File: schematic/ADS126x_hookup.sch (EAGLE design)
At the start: 13 parts, among them J1 RASPBERRYPI-40-PIN-GPIO_PTH_N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

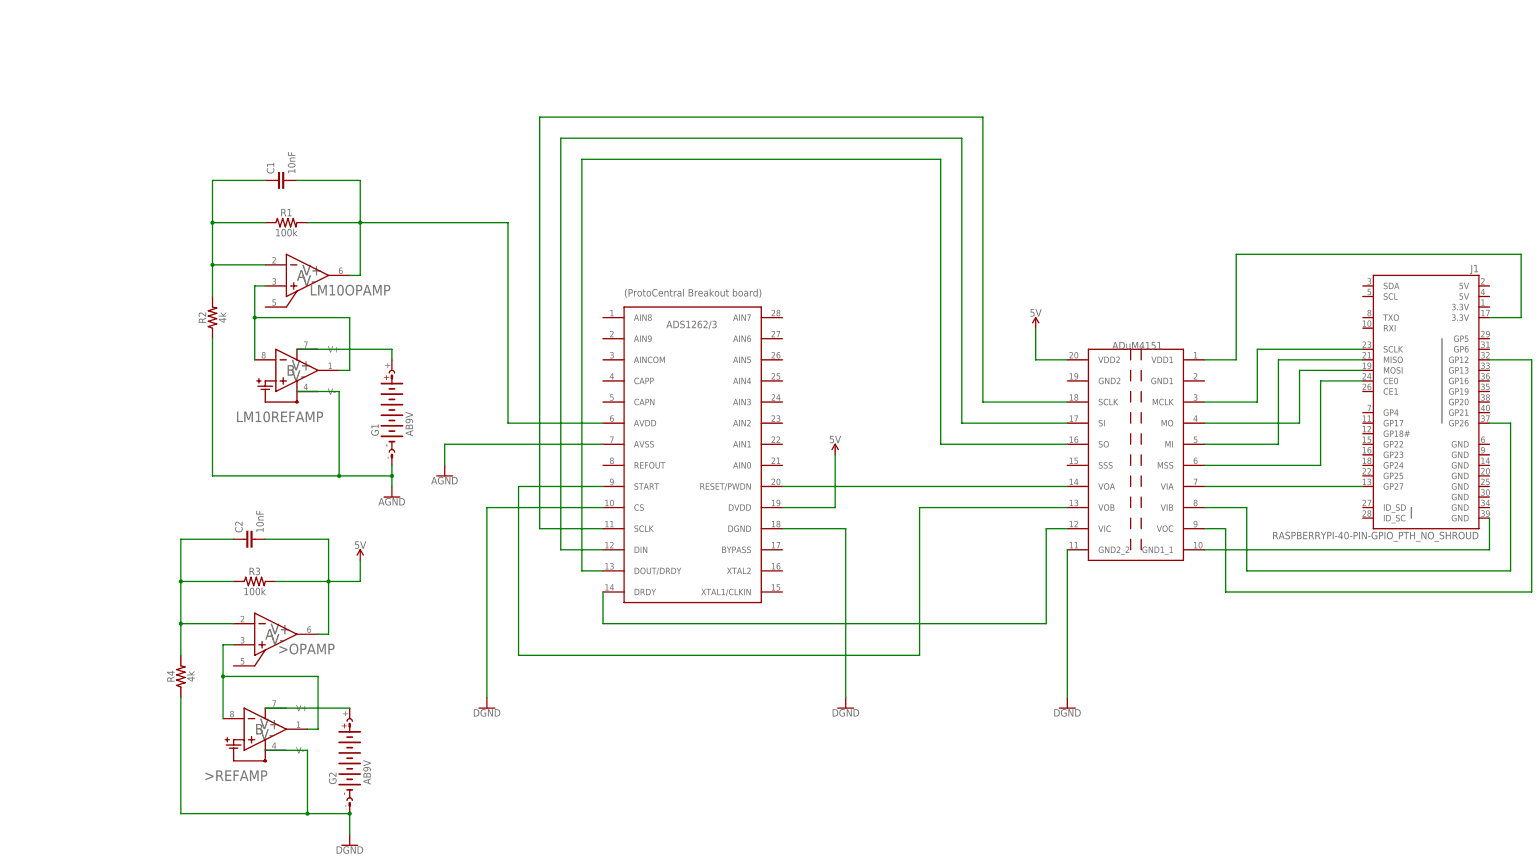
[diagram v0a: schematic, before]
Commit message: Major refactor to match Go library. updated schematic and added simplified wiring diagram
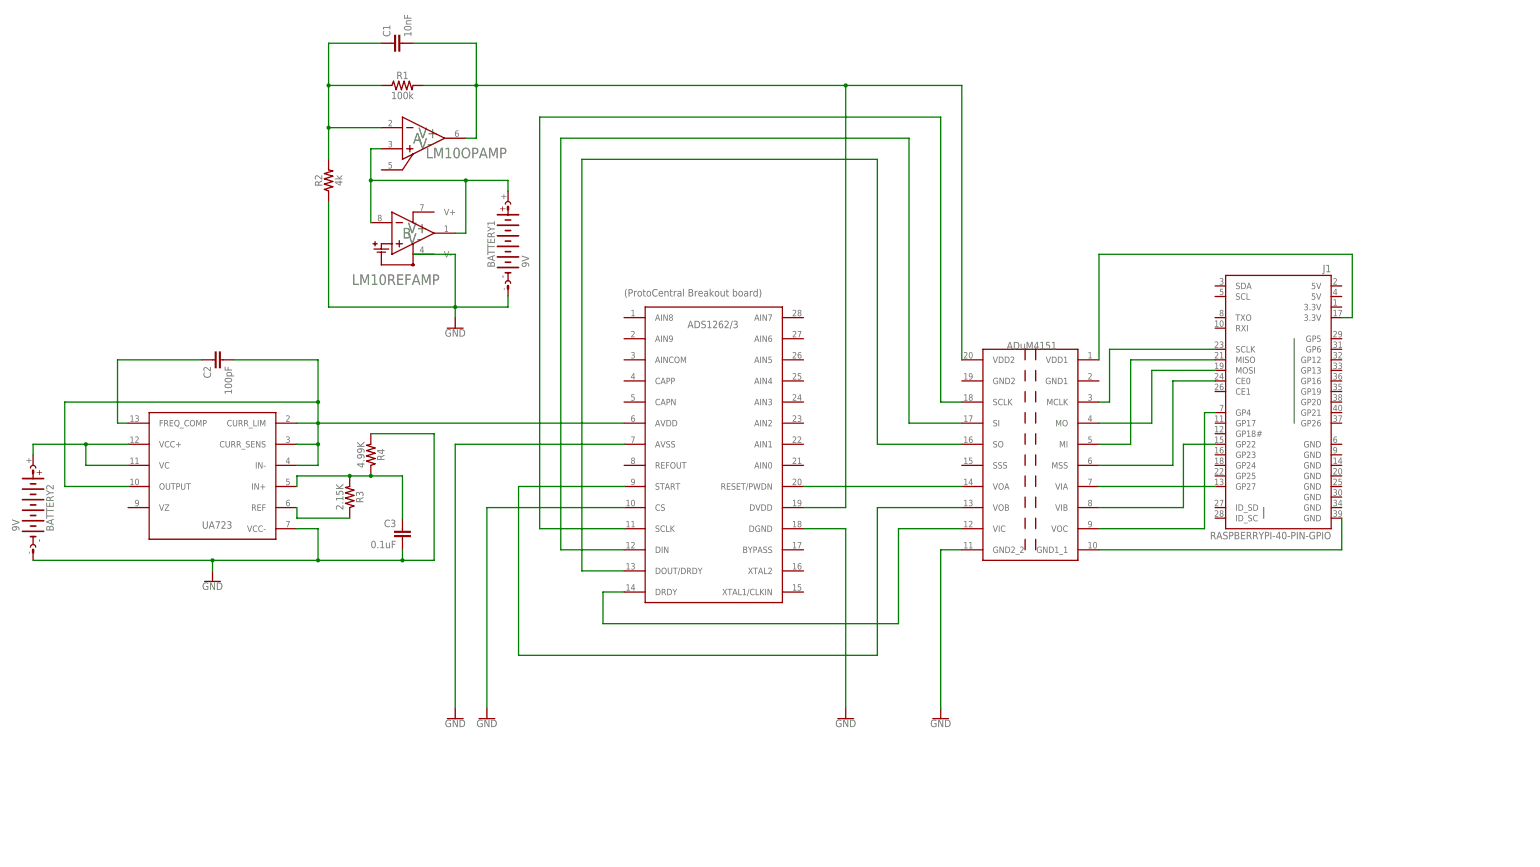
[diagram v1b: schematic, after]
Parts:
- removed >: LM10, lm10:LM10
- removed G1, G2: AB9V, battery:AB9V
- added BATTERY1, BATTERY2: 9V, battery:AB9V
- added C3: 0.1uF, SparkFun-Capacitors:0.1UF-0603-25V-5%
- added UA723: UA723, UA723:UA723
- C2: value 10nF -> 100pF; device SparkFun-Capacitors:10NF-PTH-10MM-10000V-1-% -> SparkFun-Capacitors:100PF-0603-50V-5%
- J1: value RASPBERRYPI-40-PIN-GPIO_PTH_NO_SHROUD -> RASPBERRYPI-40-PIN-GPIO
- R3: value 100k -> 2.15K; device SparkFun-Resistors:100KOHM-HORIZ-1/4W-1% -> SparkFun-Resistors:RESISTORAXIAL-0.3
- R4: value 4k -> 4.99K
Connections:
- removed net 5V: >OPAMP.OUT, C2.2, R3.2, U$1.DVDD, U$2.VDD2
- removed net N$16: LM10OPAMP.IN+, LM10REFAMP.REF_FBK, LM10REFAMP.REF_OUT
- removed net N$18: >REFAMP.V+, G2.+
- removed net N$20 (its old number): >OPAMP.IN+, >REFAMP.REF_FBK, >REFAMP.REF_OUT
- removed net N$21: >OPAMP.IN-, C2.1, R3.1, R4.2
- new net N$23: BATTERY2.+, UA723.VC, UA723.VCC+
- new net N$24: C2.2, U$1.AVDD, UA723.CURR_LIM, UA723.CURR_SENS, UA723.IN-, UA723.OUTPUT
- new net N$25: C2.1, UA723.FREQ_COMP
- new net N$26: R3.1, UA723.REF
- new net N$27: C3.1, R3.2, R4.1, UA723.IN+
- net GND: now also BATTERY1.-, BATTERY2.-, C3.2, R4.2, UA723.VCC-; no longer >REFAMP.V-, G1.-, G2.-, R4.1
- net N$14: now also J1.GP22; no longer J1.GP26
- net N$15: now also J1.GP4; no longer J1.GP12
- net N$19: now also BATTERY1.+, LM10OPAMP.IN+, LM10REFAMP.REF_FBK, LM10REFAMP.REF_OUT; no longer C1.2, LM10OPAMP.OUT, R1.2, U$1.AVDD
- net N$22: now also C1.2, LM10OPAMP.OUT, R1.2, U$1.DVDD, U$2.VDD2; no longer G1.+, LM10REFAMP.V+
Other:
- note added: "UA723"
- moved on the sheet: C1, C2, J1, LM10OPAMP, LM10REFAMP, R1, R2, R3, R4
